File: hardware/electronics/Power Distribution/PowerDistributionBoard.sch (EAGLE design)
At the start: 74 parts, among them IC1 LM556D, IC2 74AHC1G02DBV, IC3 74AHC1G02DBV, K1 EC2-12TNU, U1 IPS6041G, U2 IPS6041G, U3 V_REG_317SMD

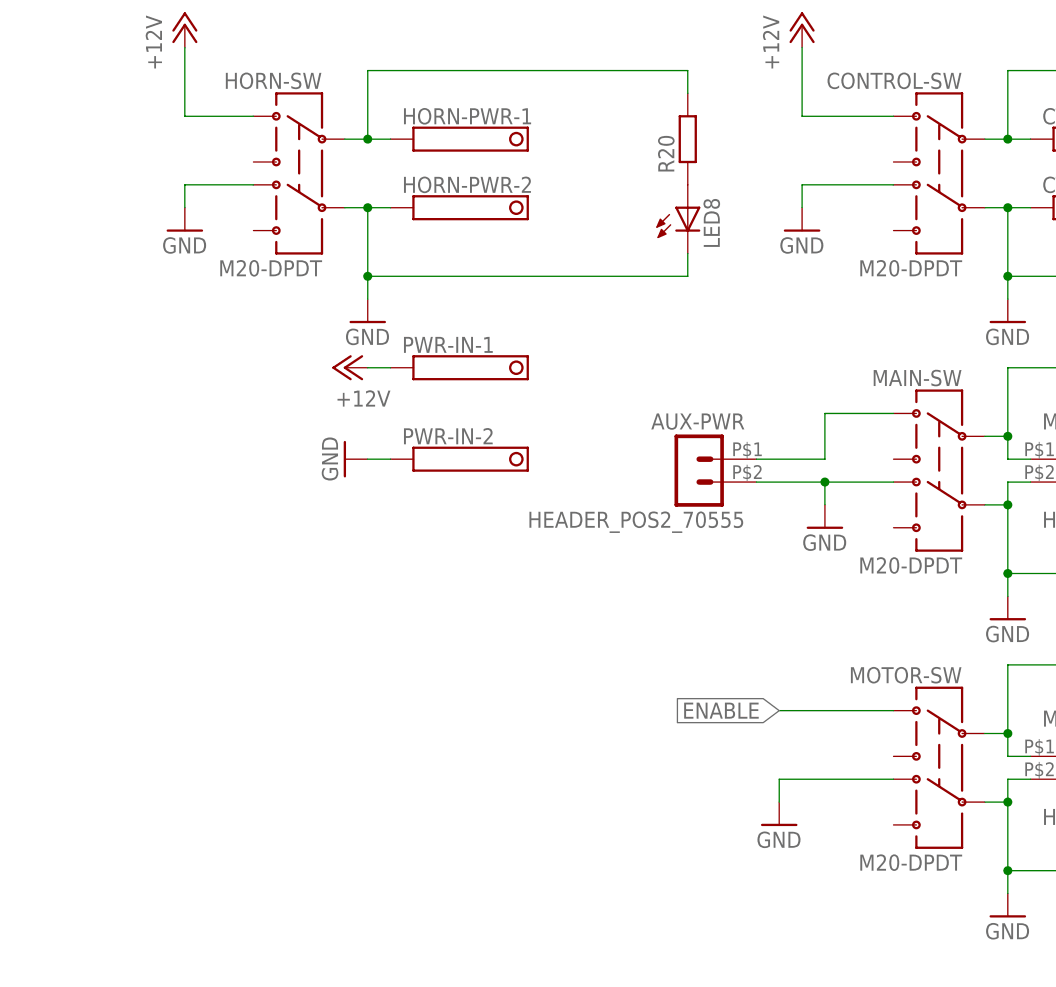
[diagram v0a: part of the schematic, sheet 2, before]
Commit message: Changed the R/C input over to SBUS. Updates to the PowerDistributionBaord
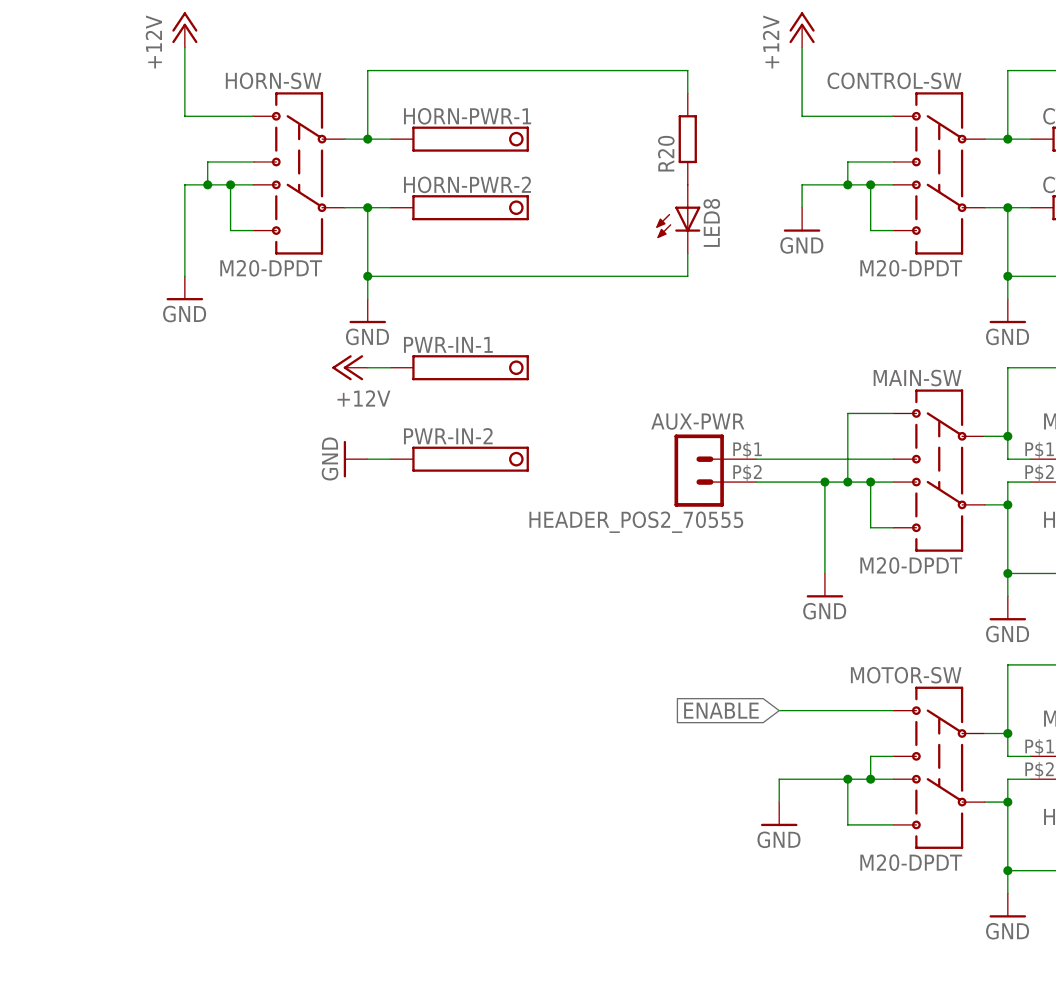
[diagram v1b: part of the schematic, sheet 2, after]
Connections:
- net GND: now also CONTROL-SW.3, CONTROL-SW.6, HORN-SW.3, HORN-SW.6, MAIN-SW.1, MAIN-SW.6, MOTOR-SW.3, MOTOR-SW.6
- net N$34: now also MAIN-SW.3; no longer MAIN-SW.1
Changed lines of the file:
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@@
 <instance part="R17" gate="G$1" x="248.92" y="157.48" rot="R90"/>
 <instance part="P+11" gate="1" x="139.7" y="165.1" rot="R90"/>
-<instance part="GND14" gate="1" x="193.04" y="147.32"/>
+<instance part="GND14" gate="1" x="193.04" y="139.7"/>
 <instance part="LED6" gate="G$1" x="248.92" y="182.88"/>
 <instance part="R18" gate="G$1" x="248.92" y="190.5" rot="R90"/>
@@
 <instance part="R20" gate="G$1" x="177.8" y="190.5" rot="R90"/>
 <instance part="P+12" gate="1" x="121.92" y="203.2"/>
-<instance part="GND15" gate="1" x="121.92" y="180.34"/>
+<instance part="GND15" gate="1" x="121.92" y="172.72"/>
 <instance part="P+13" gate="1" x="190.5" y="203.2"/>
 <instance part="GND16" gate="1" x="190.5" y="180.34"/>
@@
 <net name="GND" class="0">
 <segment>
-<pinref part="MAIN" gate="-SW" pin="4"/>
 <pinref part="GND14" gate="1" pin="GND"/>
-<wire x1="200.66" y1="152.4" x2="193.04" y2="152.4" width="0.1524" layer="91"/>
-<wire x1="193.04" y1="152.4" x2="193.04" y2="149.86" width="0.1524" layer="91"/>
+<wire x1="198.12" y1="152.4" x2="195.58" y2="152.4" width="0.1524" layer="91"/>
+<wire x1="195.58" y1="152.4" x2="193.04" y2="152.4" width="0.1524" layer="91"/>
+<wire x1="193.04" y1="152.4" x2="193.04" y2="142.24" width="0.1524" layer="91"/>
 <pinref part="AUX-PWR" gate="G$1" pin="2"/>
 <wire x1="185.42" y1="152.4" x2="193.04" y2="152.4" width="0.1524" layer="91"/>
 <junction x="193.04" y="152.4"/>
+<pinref part="MAIN" gate="-SW" pin="6"/>
+<wire x1="200.66" y1="147.32" x2="198.12" y2="147.32" width="0.1524" layer="91"/>
+<wire x1="198.12" y1="147.32" x2="198.12" y2="152.4" width="0.1524" layer="91"/>
+<pinref part="MAIN" gate="-SW" pin="4"/>
+<wire x1="200.66" y1="152.4" x2="198.12" y2="152.4" width="0.1524" layer="91"/>
+<junction x="198.12" y="152.4"/>
+<pinref part="MAIN" gate="-SW" pin="1"/>
+<wire x1="200.66" y1="160.02" x2="195.58" y2="160.02" width="0.1524" layer="91"/>
+<wire x1="195.58" y1="160.02" x2="195.58" y2="152.4" width="0.1524" layer="91"/>
+<junction x="195.58" y="152.4"/>
 </segment>
 <segment>
 <pinref part="HORN" gate="-SW" pin="4"/>
 <pinref part="GND15" gate="1" pin="GND"/>
-<wire x1="129.54" y1="185.42" x2="121.92" y2="185.42" width="0.1524" layer="91"/>
-<wire x1="121.92" y1="185.42" x2="121.92" y2="182.88" width="0.1524" layer="91"/>
+<wire x1="129.54" y1="185.42" x2="127" y2="185.42" width="0.1524" layer="91"/>
+<wire x1="124.46" y1="185.42" x2="121.92" y2="185.42" width="0.1524" layer="91"/>
+<wire x1="121.92" y1="185.42" x2="121.92" y2="175.26" width="0.1524" layer="91"/>
+<pinref part="HORN" gate="-SW" pin="3"/>
+<wire x1="129.54" y1="187.96" x2="124.46" y2="187.96" width="0.1524" layer="91"/>
+<wire x1="124.46" y1="187.96" x2="124.46" y2="185.42" width="0.1524" layer="91"/>
+<wire x1="124.46" y1="185.42" x2="127" y2="185.42" width="0.1524" layer="91"/>
+<wire x1="127" y1="185.42" x2="127" y2="180.34" width="0.1524" layer="91"/>
+<pinref part="HORN" gate="-SW" pin="6"/>
+<wire x1="127" y1="180.34" x2="129.54" y2="180.34" width="0.1524" layer="91"/>
+<junction x="124.46" y="185.42"/>
+<junction x="127" y="185.42"/>
 </segment>
 <segment>
 <pinref part="CONTROL" gate="-SW" pin="4"/>
-<wire x1="190.5" y1="185.42" x2="200.66" y2="185.42" width="0.1524" layer="91"/>
+<wire x1="190.5" y1="185.42" x2="195.58" y2="185.42" width="0.1524" layer="91"/>
+<wire x1="195.58" y1="185.42" x2="198.12" y2="185.42" width="0.1524" layer="91"/>
+<wire x1="198.12" y1="185.42" x2="200.66" y2="185.42" width="0.1524" layer="91"/>
 <wire x1="190.5" y1="182.88" x2="190.5" y2="185.42" width="0.1524" layer="91"/>
 <pinref part="GND16" gate="1" pin="GND"/>
+<pinref part="CONTROL" gate="-SW" pin="6"/>
+<wire x1="200.66" y1="180.34" x2="198.12" y2="180.34" width="0.1524" layer="91"/>
+<wire x1="198.12" y1="180.34" x2="198.12" y2="185.42" width="0.1524" layer="91"/>
+<pinref part="CONTROL" gate="-SW" pin="3"/>
+<wire x1="200.66" y1="187.96" x2="195.58" y2="187.96" width="0.1524" layer="91"/>
+<wire x1="195.58" y1="187.96" x2="195.58" y2="185.42" width="0.1524" layer="91"/>
+<junction x="198.12" y="185.42"/>
+<junction x="195.58" y="185.42"/>
 </segment>
 <segment>
@@
 <pinref part="MOTOR" gate="-SW" pin="4"/>
 <pinref part="GND18" gate="1" pin="GND"/>
-<wire x1="200.66" y1="119.38" x2="187.96" y2="119.38" width="0.1524" layer="91"/>
+<wire x1="200.66" y1="119.38" x2="198.12" y2="119.38" width="0.1524" layer="91"/>
+<wire x1="198.12" y1="119.38" x2="195.58" y2="119.38" width="0.1524" layer="91"/>
+<wire x1="195.58" y1="119.38" x2="187.96" y2="119.38" width="0.1524" layer="91"/>
 <wire x1="187.96" y1="119.38" x2="187.96" y2="116.84" width="0.1524" layer="91"/>
+<junction x="198.12" y="119.38"/>
+<junction x="195.58" y="119.38"/>
+<pinref part="MOTOR" gate="-SW" pin="3"/>
+<wire x1="200.66" y1="121.92" x2="198.12" y2="121.92" width="0.1524" layer="91"/>
+<wire x1="198.12" y1="121.92" x2="198.12" y2="119.38" width="0.1524" layer="91"/>
+<pinref part="MOTOR" gate="-SW" pin="6"/>
+<wire x1="200.66" y1="114.3" x2="195.58" y2="114.3" width="0.1524" layer="91"/>
+<wire x1="195.58" y1="114.3" x2="195.58" y2="119.38" width="0.1524" layer="91"/>
 </segment>
 <segment>
@@
 <net name="N$34" class="0">
 <segment>
-<pinref part="MAIN" gate="-SW" pin="1"/>
-<wire x1="200.66" y1="160.02" x2="193.04" y2="160.02" width="0.1524" layer="91"/>
-<wire x1="193.04" y1="160.02" x2="193.04" y2="154.94" width="0.1524" layer="91"/>
 <pinref part="AUX-PWR" gate="G$1" pin="1"/>
-<wire x1="193.04" y1="154.94" x2="185.42" y2="154.94" width="0.1524" layer="91"/>
-</segment>
-</net>
+<pinref part="MAIN" gate="-SW" pin="3"/>
+<wire x1="200.66" y1="154.94" x2="185.42" y2="154.94" width="0.1524" layer="91"/>
+</segment>
+</net>

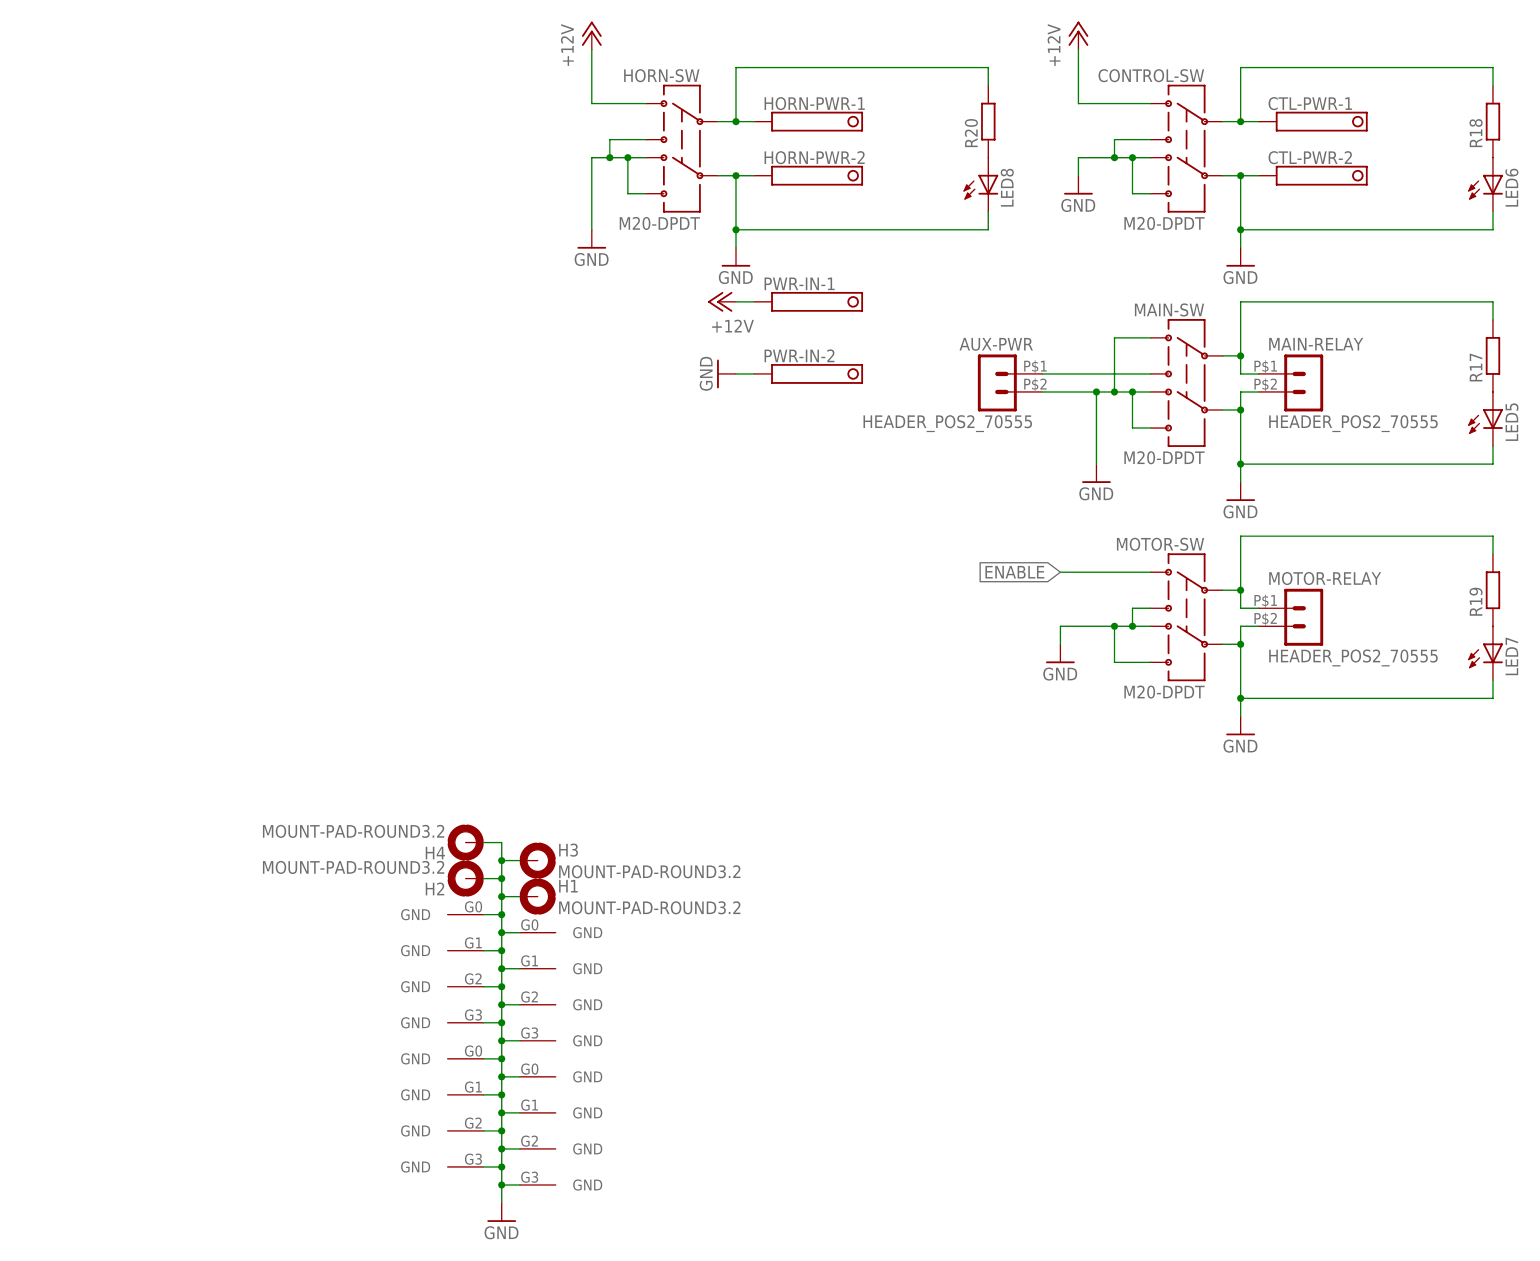
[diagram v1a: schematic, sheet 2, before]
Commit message: Making sure we have the latest board in github
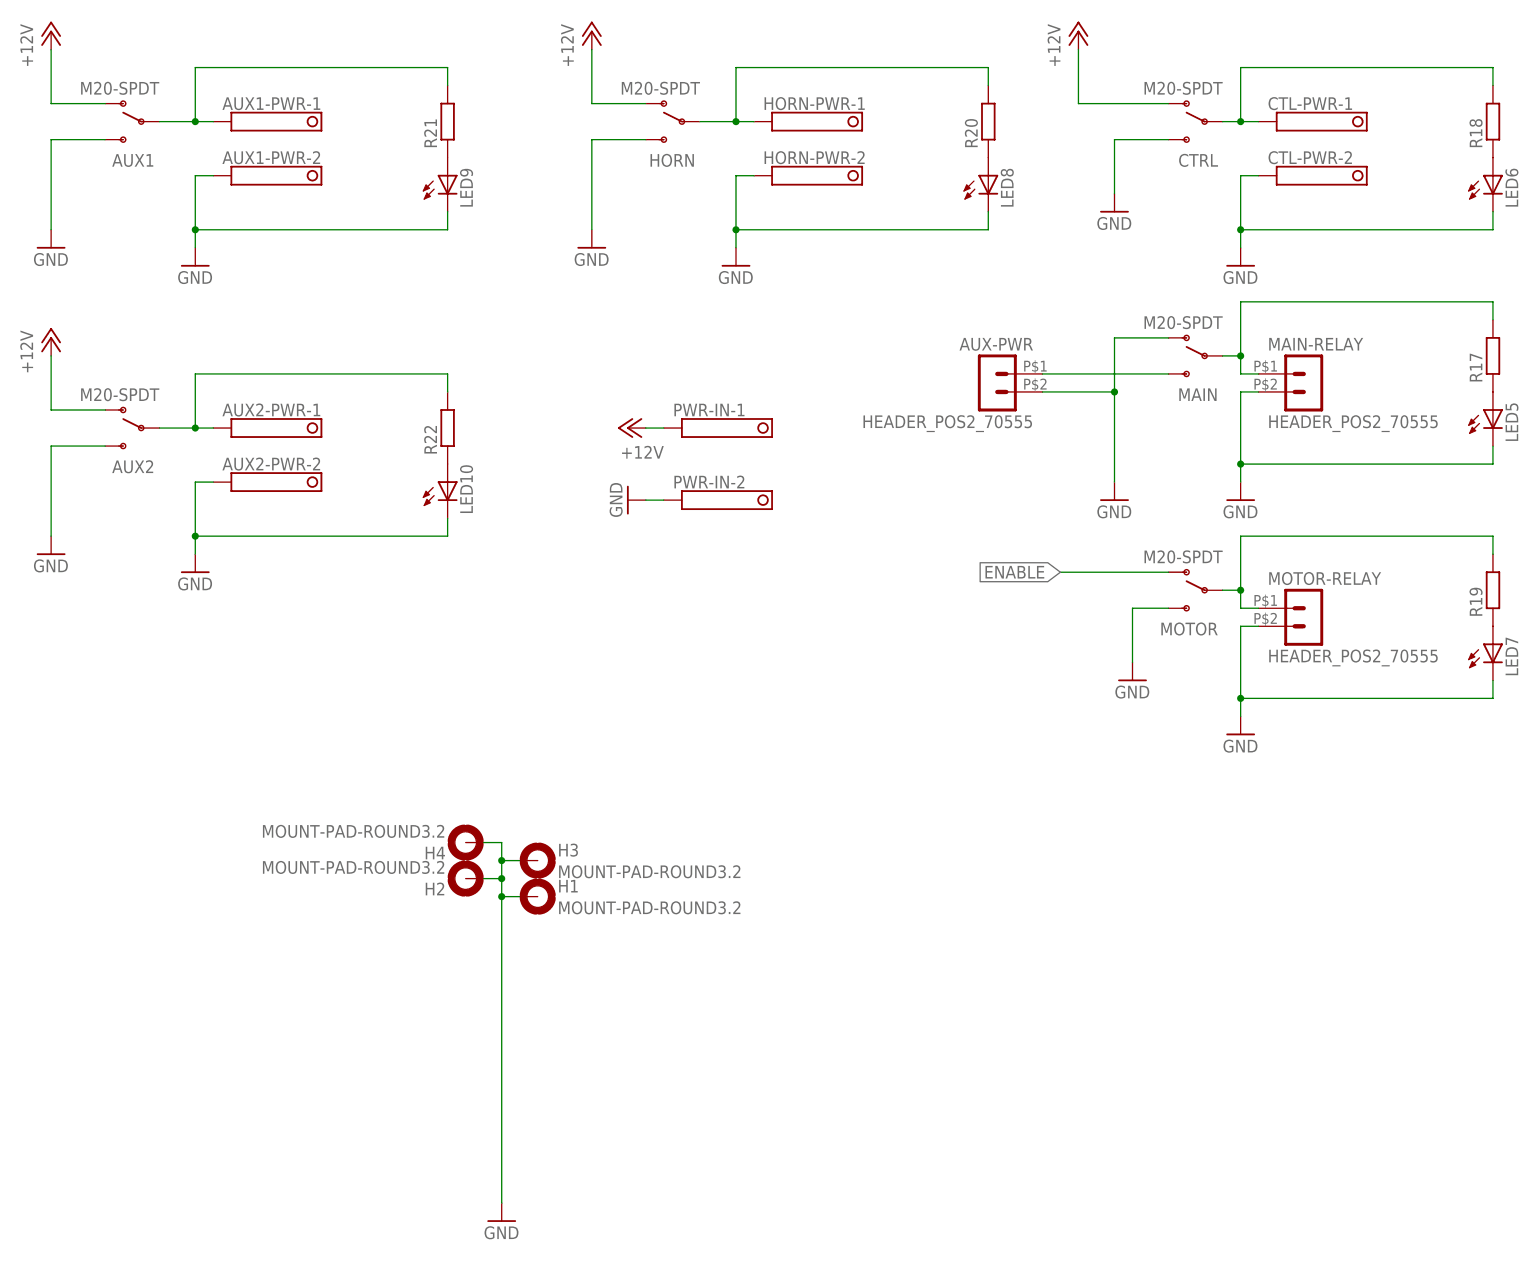
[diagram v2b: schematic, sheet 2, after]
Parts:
- removed CONTROL: M20-DPDT, logos-switch:M20-DPDT
- added AUX1, AUX2, CTRL: M20-SPDT, logos-switch:M20-SPDT
- added AUX1-PWR, AUX2-PWR: 1751248, con-phoenix-350:1751248
- added LED10, LED9: (no value), adafruit:LEDCHIP-LED0805
- added R21, R22: (no value), resistor:R-EU_R0603
- HORN, MAIN, MOTOR: value M20-DPDT -> M20-SPDT; device logos-switch:M20-DPDT -> logos-switch:M20-SPDT; PARTNO M2022LL2W13 -> (none)
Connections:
- new net N$29: AUX1-PWR-1.K, AUX1.P, R21.2
- new net N$31: LED9.A, R21.1
- new net N$37: AUX2-PWR-1.K, AUX2.P, R22.2
- new net N$39: LED10.A, R22.1
- net +12V: now also AUX1.O, AUX2.O, CTRL.O, HORN.O; no longer CONTROL-SW.1, HORN-SW.1
- net ENABLE: now also MOTOR.O; no longer MOTOR-SW.1
- net GND: now also AUX1-PWR-2.K, AUX1.S, AUX2-PWR-2.K, AUX2.S, CTRL.S, HORN.S, LED10.C, LED9.C, MAIN.O, MOTOR.S; no longer CONTROL-SW.3, CONTROL-SW.4, CONTROL-SW.5, CONTROL-SW.6, CONTROLG$2.GND, CONTROLG$3.GND, CONTROLG$4.GND, CONTROLG$5.GND, HORN-SW.3, HORN-SW.4, HORN-SW.5, HORN-SW.6, HORNG$2.GND, HORNG$3.GND, HORNG$4.GND, HORNG$5.GND, MAIN-SW.1, MAIN-SW.4, MAIN-SW.5, MAIN-SW.6, MAING$2.GND, MAING$3.GND, MAING$4.GND, MAING$5.GND, MOTOR-SW.3, MOTOR-SW.4, MOTOR-SW.5, MOTOR-SW.6, MOTORG$2.GND, MOTORG$3.GND, MOTORG$4.GND, MOTORG$5.GND
- net N$33: now also HORN.P; no longer HORN-SW.2
- net N$34: now also MAIN.S; no longer MAIN-SW.3
- net N$36: now also MOTOR.P; no longer MOTOR-SW.2
- net N$38: now also CTRL.P; no longer CONTROL-SW.2
- net N$41: now also MAIN.P; no longer MAIN-SW.2
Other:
- moved on the sheet: PWR-IN-1, PWR-IN-2
